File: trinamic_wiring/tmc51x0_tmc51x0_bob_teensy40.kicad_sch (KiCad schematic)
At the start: 3 parts, among them M1 Stepper_Motor

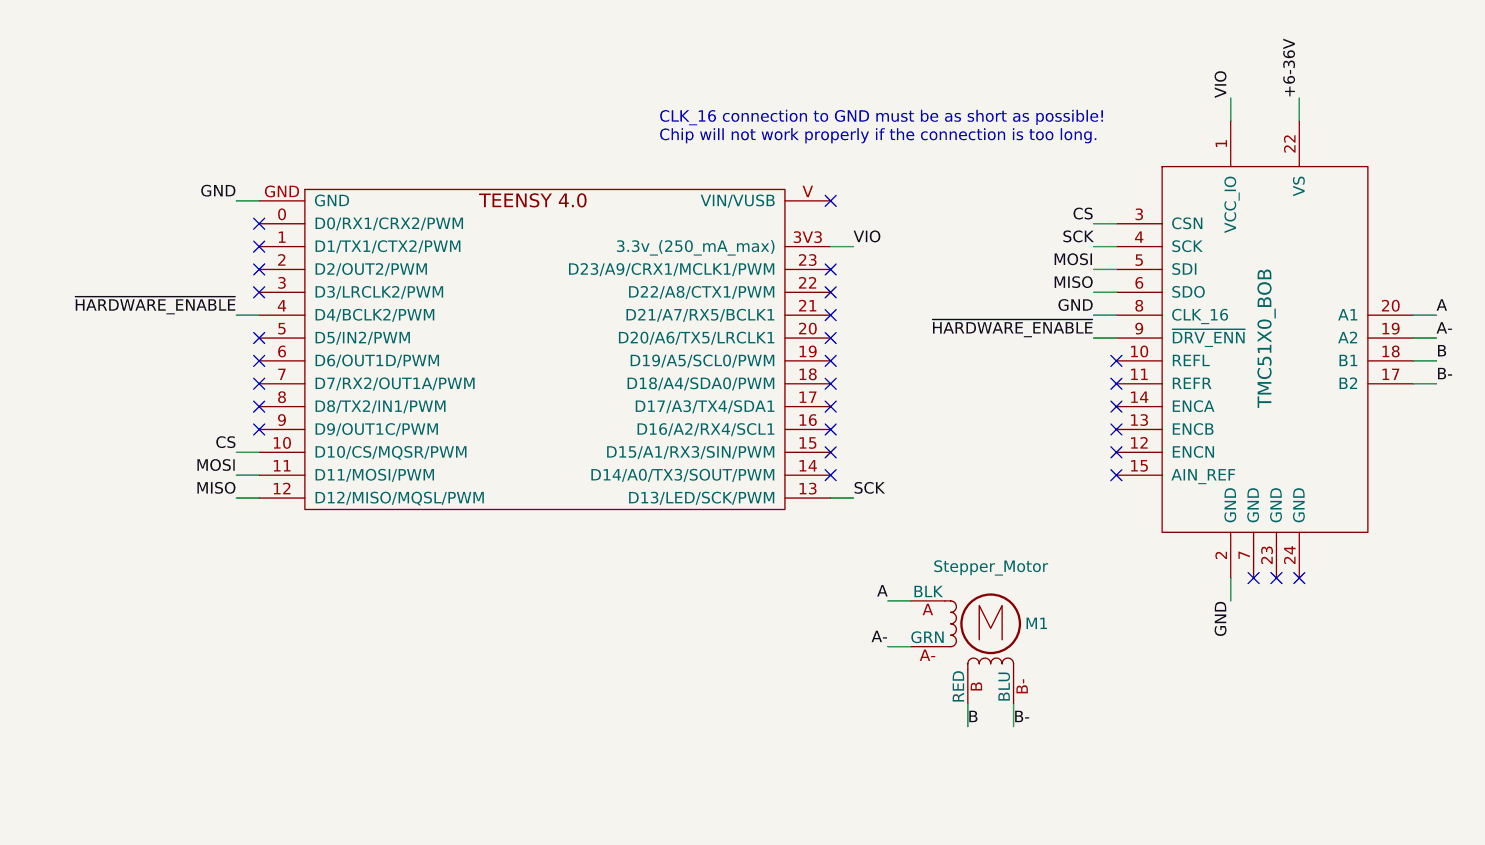
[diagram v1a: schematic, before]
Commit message: Add optional encoder to teensy example:
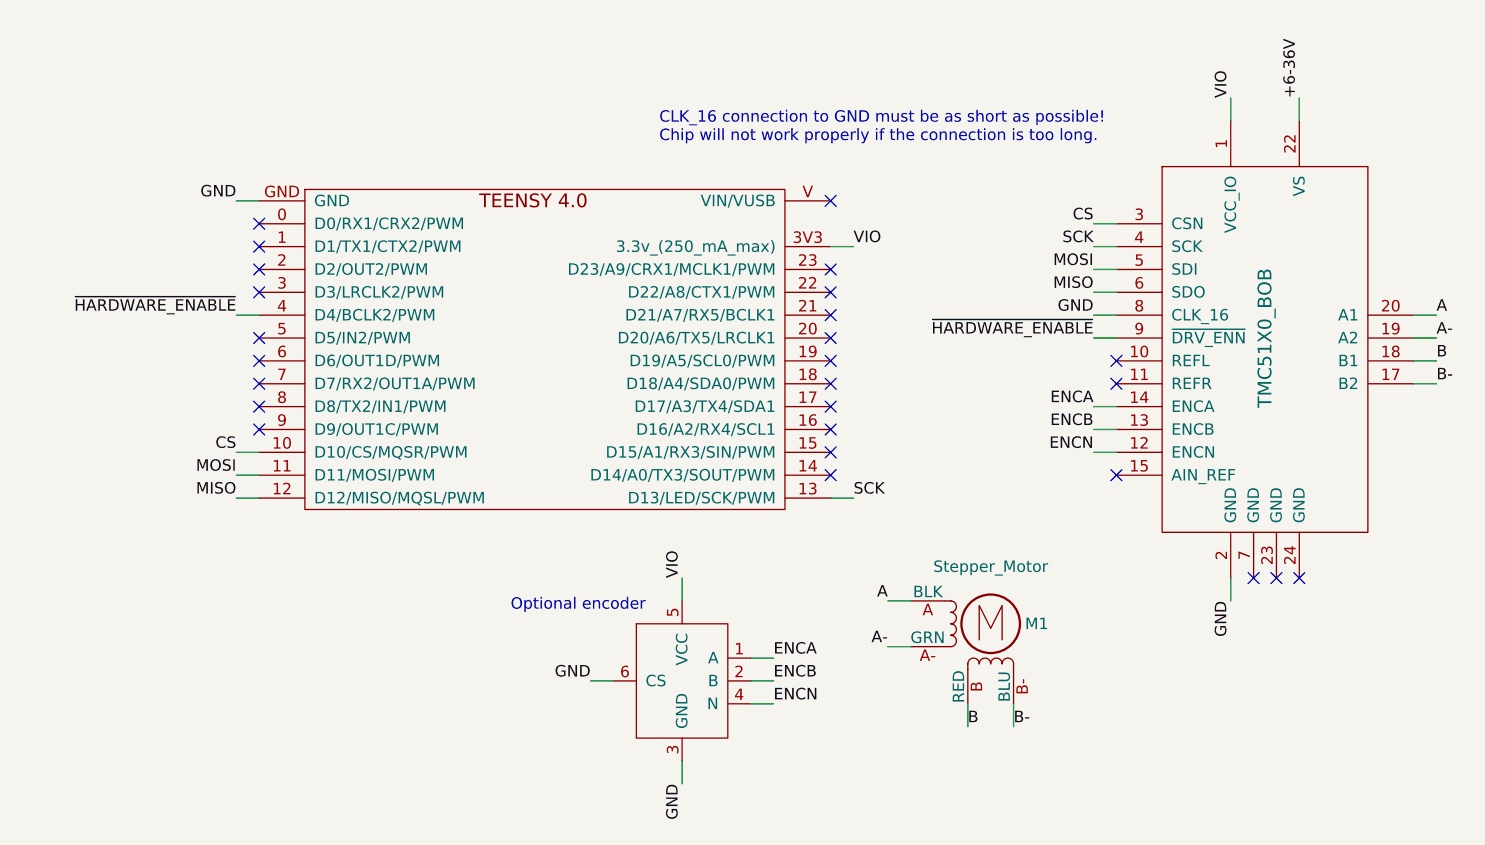
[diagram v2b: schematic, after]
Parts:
- added ENC2: ENCODER_EMS22Q, symbol Janelia:ENCODER_EMS22Q
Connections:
- net GND: now also ENC2.3 (GND), ENC2.6 (CS)
- net VIO: now also ENC2.5 (VCC)
- net ENCN: now reaches BOB1.12 (ENCN)
- net ENCN: now also ENC2.4 (N)
- net ENCB: now reaches BOB1.13 (ENCB)
- net ENCB: now also ENC2.2 (B)
- net ENCA: now reaches BOB1.14 (ENCA)
- net ENCA: now also ENC2.1 (A)
- no-connect marks 29 -> 26
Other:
- note added: "Optional encoder"
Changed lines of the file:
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@@
   (no_connect (at 132.08 86.36))
   (no_connect (at 132.08 114.3))
-  (no_connect (at 163.83 114.3))
   (no_connect (at 163.83 104.14))
-  (no_connect (at 163.83 109.22))
   (no_connect (at 163.83 106.68))
   (no_connect (at 181.61 128.27))
@@
   (no_connect (at 132.08 99.06))
   (no_connect (at 68.58 93.98))
-  (no_connect (at 163.83 111.76))
   (no_connect (at 132.08 116.84))
   (no_connect (at 179.07 128.27))
@@
     (stroke (width 0) (type default))
   )
+  (wire (pts (xy 123.19 142.24) (xy 125.73 142.24))
+    (stroke (width 0) (type default))
+  )
   (wire (pts (xy 66.04 116.84) (xy 68.58 116.84))
     (stroke (width 0) (type default))
@@
     (stroke (width 0) (type default))
   )
+  (wire (pts (xy 123.19 137.16) (xy 125.73 137.16))
+    (stroke (width 0) (type default))
+  )
+  (wire (pts (xy 123.19 139.7) (xy 125.73 139.7))
+    (stroke (width 0) (type default))
+  )
+  (wire (pts (xy 115.57 130.81) (xy 115.57 128.27))
+    (stroke (width 0) (type default))
+  )
   (wire (pts (xy 138.43 135.89) (xy 140.97 135.89))
     (stroke (width 0) (type default))
   )
+  (wire (pts (xy 115.57 151.13) (xy 115.57 148.59))
+    (stroke (width 0) (type default))
+  )
   (wire (pts (xy 163.83 91.44) (xy 161.29 91.44))
     (stroke (width 0) (type default))
   )
+  (wire (pts (xy 105.41 139.7) (xy 107.95 139.7))
+    (stroke (width 0) (type default))
+  )
   (wire (pts (xy 161.29 93.98) (xy 163.83 93.98))
     (stroke (width 0) (type default))
@@
     (stroke (width 0) (type default))
   )
+  (wire (pts (xy 163.83 111.76) (xy 161.29 111.76))
+    (stroke (width 0) (type default))
+  )
   (wire (pts (xy 152.4 142.24) (xy 152.4 144.78))
     (stroke (width 0) (type default))
@@
     (stroke (width 0) (type default))
   )
+  (wire (pts (xy 163.83 114.3) (xy 161.29 114.3))
+    (stroke (width 0) (type default))
+  )
   (wire (pts (xy 196.85 101.6) (xy 199.39 101.6))
     (stroke (width 0) (type default))
@@
     (stroke (width 0) (type default))
   )
+  (wire (pts (xy 163.83 109.22) (xy 161.29 109.22))
+    (stroke (width 0) (type default))
+  )
   (wire (pts (xy 163.83 99.06) (xy 161.29 99.06))
     (stroke (width 0) (type default))
@@
   (wire (pts (xy 196.85 106.68) (xy 199.39 106.68))
     (stroke (width 0) (type default))
+  )
+  (text "Optional encoder" (at 96.52 132.08 0)
+    (effects (font (size 1.27 1.27)) (justify left bottom))
   )
   (text "CLK_16 connection to GND must be as short as possible!\nChip will not work properly if the connection is too long."
@@
     (effects (font (size 1.27 1.27)) (justify left bottom))
   )
+  (label "ENCA" (at 161.29 109.22 180) (fields_autoplaced)
+    (effects (font (size 1.27 1.27)) (justify right bottom))
+  )
+  (label "ENCA" (at 125.73 137.16 0) (fields_autoplaced)
+    (effects (font (size 1.27 1.27)) (justify left bottom))
+  )
   (label "VIO" (at 176.53 74.93 90) (fields_autoplaced)
     (effects (font (size 1.27 1.27)) (justify left bottom))
@@
     (effects (font (size 1.27 1.27)) (justify right bottom))
   )
+  (label "ENCN" (at 125.73 142.24 0) (fields_autoplaced)
+    (effects (font (size 1.27 1.27)) (justify left bottom))
+  )
   (label "SCK" (at 161.29 91.44 180) (fields_autoplaced)
     (effects (font (size 1.27 1.27)) (justify right bottom))
@@
     (effects (font (size 1.27 1.27)) (justify right bottom))
   )
+  (label "GND" (at 115.57 151.13 270) (fields_autoplaced)
+    (effects (font (size 1.27 1.27)) (justify right bottom))
+  )
   (label "B-" (at 199.39 106.68 0) (fields_autoplaced)
     (effects (font (size 1.27 1.27)) (justify left bottom))
@@
     (effects (font (size 1.27 1.27)) (justify right bottom))
   )
+  (label "ENCB" (at 125.73 139.7 0) (fields_autoplaced)
+    (effects (font (size 1.27 1.27)) (justify left bottom))
+  )
   (label "A-" (at 138.43 135.89 180) (fields_autoplaced)
     (effects (font (size 1.27 1.27)) (justify right bottom))
@@
     (effects (font (size 1.27 1.27)) (justify right bottom))
   )
+  (label "ENCB" (at 161.29 111.76 180) (fields_autoplaced)
+    (effects (font (size 1.27 1.27)) (justify right bottom))
+  )
   (label "B" (at 199.39 104.14 0) (fields_autoplaced)
     (effects (font (size 1.27 1.27)) (justify left bottom))
@@
   )
   (label "GND" (at 66.04 86.36 180) (fields_autoplaced)
+    (effects (font (size 1.27 1.27)) (justify right bottom))
+  )
+  (label "VIO" (at 115.57 128.27 90) (fields_autoplaced)
+    (effects (font (size 1.27 1.27)) (justify left bottom))
+  )
+  (label "GND" (at 105.41 139.7 180) (fields_autoplaced)
+    (effects (font (size 1.27 1.27)) (justify right bottom))
+  )
+  (label "ENCN" (at 161.29 114.3 180) (fields_autoplaced)
     (effects (font (size 1.27 1.27)) (justify right bottom))
   )
@@
         )
       )
+    )
+  )
+  (symbol (lib_id "Janelia:ENCODER_EMS22Q") (at 115.57 139.7 0) (unit 1)
+    (in_bom yes) (on_board yes) (dnp no) (fields_autoplaced)
+    (property "Reference" "ENC2" (at 118.11 132.08 0)
+      (effects (font (size 1.524 1.524)) hide)
+    )
+    (property "Value" "ENCODER_EMS22Q" (at 115.57 119.38 0) (do_not_autoplace)
+      (effects (font (size 1.524 1.524)) hide)
+    )
+    (property "Footprint" "" (at 119.38 151.13 0)
+      (effects (font (size 1.524 1.524)) hide)
+    )
+    (property "Datasheet" "" (at 115.57 139.7 0)
+      (effects (font (size 1.524 1.524)))
+    )
+    (property "Vendor" "Digi-Key" (at 115.57 114.3 0)
+      (effects (font (size 1.524 1.524)) hide)
+    )
+    (property "Vendor Part Number" "EMS22Q31-B28-LS4-ND" (at 115.57 111.76 0)
+      (effects (font (size 1.524 1.524)) hide)
+    )
+    (property "Description" "ROTARY ENCODER MAGNETIC 256PPR" (at 115.57 109.22 0)
+      (effects (font (size 1.524 1.524)) hide)
+    )
+    (property "Sim.Enable" "0" (at 115.57 102.87 0)
+      (effects (font (size 1.27 1.27)) hide)
+    )
+    (property "Manufacturer" "Bourns Inc." (at 115.57 116.84 0)
+      (effects (font (size 1.27 1.27)) hide)
+    )
+    (property "Manufacturer Part Number" "EMS22Q31-B28-LS4" (at 115.57 106.68 0)
+      (effects (font (size 1.27 1.27)) hide)
+    )
+    (pin "1")
+    (pin "5")
+    (pin "4")
+    (pin "3")
+    (pin "6")
+    (pin "2")
+    (instances
+      (project "trinamic_wiring"
+        (path "/e4144788-6304-493f-818e-5d881d3b7418/a161638e-a96f-4455-865a-1d7502675f43/176cb0b5-cab1-47ac-9998-e59b71e39393/106cbaaa-dd32-4d4d-a442-e3c42a8253b0"
+          (reference "ENC2") (unit 1)
+        )
+      )
